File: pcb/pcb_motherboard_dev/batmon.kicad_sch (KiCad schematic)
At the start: 15 parts, among them U9 MCP6002-xSN

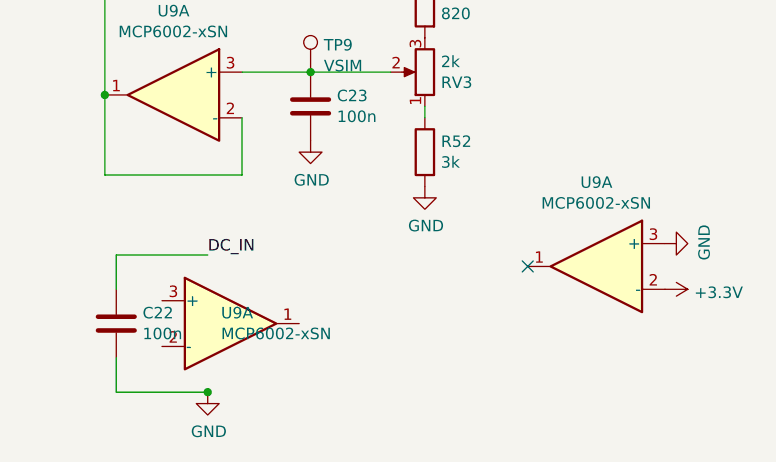
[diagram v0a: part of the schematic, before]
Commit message: PCB MB-DEV update
+Added a jumper for GPIO12 for flashing and setting efuse for 3.3 Flash operation
+Added Text Variables to Schematic and PCB
+introduced versioning of pcb
+added filenames and version to schematic sheets
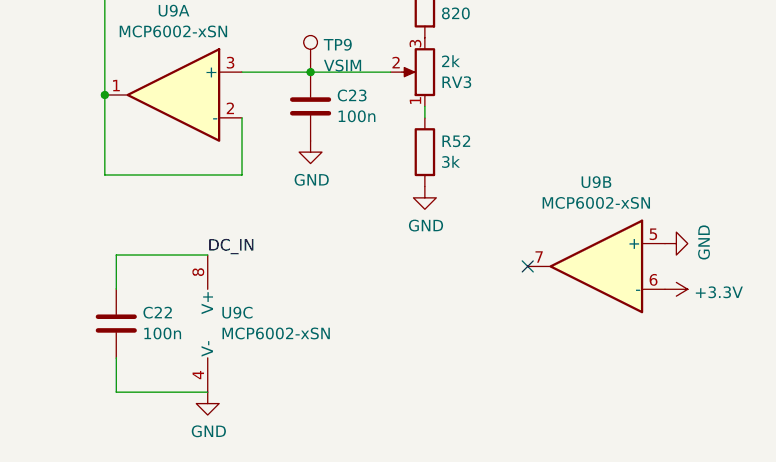
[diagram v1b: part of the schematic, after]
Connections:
- net +3V3: now also U9.6 (-); no longer U9.2 (-)
- net DC_IN: now also U9.8 (V+)
- net GND: now also U9.4 (V-), U9.5 (+); no longer U9.3 (+)
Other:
- title: (none) -> ForcelogADC_MB-DEV_v${VERSION}
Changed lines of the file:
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@@
 (kicad_sch (version 20211123) (generator eeschema)
   (paper "A4")
+  (title_block
+    (title "ForcelogADC_MB-DEV_v${VERSION}")
+    (rev "${REVISION}")
+  )
   (junction (at 105.41 88.9) (diameter 0) (color 0 0 0 0)
   )
@@
   )
   (junction (at 142.24 92.71) (diameter 0) (color 0 0 0 0)
-  )
-  (junction (at 153.67 125.73) (diameter 0) (color 0 0 0 0)
   )
   (no_connect (at 189.23 111.76))
@@
     (pin "1")
   )
-  (symbol (lib_id "Amplifier_Operational:MCP6002-xSN") (at 196.85 111.76 0) (mirror y)
+  (symbol (lib_id "Amplifier_Operational:MCP6002-xSN") (at 196.85 111.76 0) (mirror y) (unit 2)
     (in_bom yes) (on_board yes)
     (property "Reference" "U9" (id 0) (at 196.85 102.4382 0))
@@
       (effects (font (size 1.27 1.27)) hide)
     )
+    (pin "1")
+    (pin "2")
+    (pin "3")
     (pin "5")
     (pin "6")
     (pin "7")
-  )
-  (symbol (lib_id "power:GND") (at 204.47 109.22 90)
+    (pin "4")
+    (pin "8")
+  )
+  (symbol (lib_id "power:GND") (at 204.47 109.22 90) (unit 1)
     (in_bom yes) (on_board yes)
     (property "Reference" "#PWR0148" (id 0) (at 210.82 109.22 0)
@@
     (pin "1")
   )
-  (symbol (lib_id "Device:D_Schottky_Dual_Series_AKC") (at 105.41 83.82 0) (mirror y)
+  (symbol (lib_id "Device:D_Schottky_Dual_Series_AKC") (at 105.41 83.82 0) (mirror y) (unit 1)
     (in_bom yes) (on_board yes)
     (property "Reference" "D12" (id 0) (at 105.41 81.788 90)
@@
     (pin "3")
   )
-  (symbol (lib_id "power:GND") (at 113.03 83.82 90)
+  (symbol (lib_id "power:GND") (at 113.03 83.82 90) (unit 1)
     (in_bom yes) (on_board yes)
     (property "Reference" "#PWR0144" (id 0) (at 119.38 83.82 0)
@@
     (pin "1")
   )
-  (symbol (lib_id "Connector:TestPoint") (at 95.25 88.9 180)
+  (symbol (lib_id "Connector:TestPoint") (at 95.25 88.9 180) (unit 1)
     (in_bom yes) (on_board yes)
     (property "Reference" "TP8" (id 0) (at 96.7232 89.5604 0)
@@
     (pin "1")
   )
-  (symbol (lib_id "Connector:TestPoint") (at 165.1 90.17 0)
+  (symbol (lib_id "Connector:TestPoint") (at 165.1 90.17 0) (unit 1)
     (in_bom yes) (on_board yes)
     (property "Reference" "TP9" (id 0) (at 166.5732 87.1728 0)
@@
     (pin "1")
   )
-  (symbol (lib_id "Device:R") (at 121.92 82.55 0)
+  (symbol (lib_id "Device:R") (at 121.92 82.55 0) (unit 1)
     (in_bom yes) (on_board yes)
     (property "Reference" "R38" (id 0) (at 123.698 81.3816 0)
@@
     (pin "2")
   )
-  (symbol (lib_id "Device:R") (at 121.92 92.71 0)
+  (symbol (lib_id "Device:R") (at 121.92 92.71 0) (unit 1)
     (in_bom yes) (on_board yes)
     (property "Reference" "R39" (id 0) (at 123.698 91.5416 0)
@@
     (pin "2")
   )
-  (symbol (lib_id "Device:C") (at 110.49 92.71 0)
+  (symbol (lib_id "Device:C") (at 110.49 92.71 0) (unit 1)
     (in_bom yes) (on_board yes)
     (property "Reference" "C17" (id 0) (at 113.411 91.5416 0)
@@
     (pin "2")
   )
-  (symbol (lib_id "power:GND") (at 118.11 96.52 0)
+  (symbol (lib_id "power:GND") (at 118.11 96.52 0) (unit 1)
     (in_bom yes) (on_board yes)
     (property "Reference" "#PWR074" (id 0) (at 118.11 102.87 0)
@@
     (pin "1")
   )
-  (symbol (lib_id "Amplifier_Operational:MCP6002-xSN") (at 149.86 92.71 0) (mirror y)
+  (symbol (lib_id "Amplifier_Operational:MCP6002-xSN") (at 149.86 92.71 0) (mirror y) (unit 1)
     (in_bom yes) (on_board yes)
     (property "Reference" "U9" (id 0) (at 149.86 83.3882 0))
@@
     (pin "2")
     (pin "3")
-  )
-  (symbol (lib_id "Amplifier_Operational:MCP6002-xSN") (at 156.21 118.11 0)
-    (in_bom yes) (on_board yes)
-    (property "Reference" "U9" (id 0) (at 155.1432 116.9416 0)
-      (effects (font (size 1.27 1.27)) (justify left))
-    )
-    (property "Value" "MCP6002-xSN" (id 1) (at 155.1432 119.253 0)
-      (effects (font (size 1.27 1.27)) (justify left))
-    )
-    (property "Footprint" "Package_SO:SO-8_3.9x4.9mm_P1.27mm" (id 2) (at 156.21 118.11 0)
-      (effects (font (size 1.27 1.27)) hide)
-    )
-    (property "Datasheet" "http://ww1.microchip.com/downloads/en/DeviceDoc/21733j.pdf" (id 3) (at 156.21 118.11 0)
-      (effects (font (size 1.27 1.27)) hide)
-    )
-    (property "LCSC" "C7377" (id 4) (at 156.21 118.11 0)
-      (effects (font (size 1.27 1.27)) hide)
-    )
-    (property "Digikey" "MCP6002-I/SN-ND" (id 5) (at 156.21 118.11 0)
-      (effects (font (size 1.27 1.27)) hide)
-    )
+    (pin "5")
+    (pin "6")
+    (pin "7")
     (pin "4")
     (pin "8")
   )
-  (symbol (lib_id "Jumper:Jumper_3_Open") (at 121.92 74.93 0)
+  (symbol (lib_id "Amplifier_Operational:MCP6002-xSN") (at 156.21 118.11 0) (unit 3)
+    (in_bom yes) (on_board yes)
+    (property "Reference" "U9" (id 0) (at 155.1432 116.9416 0)
+      (effects (font (size 1.27 1.27)) (justify left))
+    )
+    (property "Value" "MCP6002-xSN" (id 1) (at 155.1432 119.253 0)
+      (effects (font (size 1.27 1.27)) (justify left))
+    )
+    (property "Footprint" "Package_SO:SO-8_3.9x4.9mm_P1.27mm" (id 2) (at 156.21 118.11 0)
+      (effects (font (size 1.27 1.27)) hide)
+    )
+    (property "Datasheet" "http://ww1.microchip.com/downloads/en/DeviceDoc/21733j.pdf" (id 3) (at 156.21 118.11 0)
+      (effects (font (size 1.27 1.27)) hide)
+    )
+    (property "LCSC" "C7377" (id 4) (at 156.21 118.11 0)
+      (effects (font (size 1.27 1.27)) hide)
+    )
+    (property "Digikey" "MCP6002-I/SN-ND" (id 5) (at 156.21 118.11 0)
+      (effects (font (size 1.27 1.27)) hide)
+    )
+    (pin "1")
+    (pin "2")
+    (pin "3")
+    (pin "5")
+    (pin "6")
+    (pin "7")
+    (pin "4")
+    (pin "8")
+  )
+  (symbol (lib_id "Jumper:Jumper_3_Open") (at 121.92 74.93 0) (unit 1)
     (in_bom yes) (on_board yes)
     (property "Reference" "JP3" (id 0) (at 121.92 71.5518 0))
@@
     (pin "3")
   )
-  (symbol (lib_id "Device:R_Potentiometer") (at 177.8 90.17 180)
+  (symbol (lib_id "Device:R_Potentiometer") (at 177.8 90.17 180) (unit 1)
     (in_bom yes) (on_board yes)
     (property "Reference" "RV3" (id 0) (at 179.578 91.3384 0)
@@
     (pin "3")
   )
-  (symbol (lib_id "Device:R") (at 177.8 82.55 0) (mirror y)
+  (symbol (lib_id "Device:R") (at 177.8 82.55 0) (mirror y) (unit 1)
     (in_bom yes) (on_board yes)
     (property "Reference" "R51" (id 0) (at 179.578 81.3816 0)
@@
     (pin "2")
   )
-  (symbol (lib_id "Device:R") (at 177.8 99.06 0) (mirror y)
+  (symbol (lib_id "Device:R") (at 177.8 99.06 0) (mirror y) (unit 1)
     (in_bom yes) (on_board yes)
     (property "Reference" "R52" (id 0) (at 179.578 97.8916 0)
@@
     (pin "2")
   )
-  (symbol (lib_id "power:GND") (at 177.8 102.87 0)
+  (symbol (lib_id "power:GND") (at 177.8 102.87 0) (unit 1)
     (in_bom yes) (on_board yes)
     (property "Reference" "#PWR083" (id 0) (at 177.8 109.22 0)
@@
     (pin "1")
   )
-  (symbol (lib_id "power:GND") (at 153.67 125.73 0)
+  (symbol (lib_id "power:GND") (at 153.67 125.73 0) (unit 1)
     (in_bom yes) (on_board yes)
     (property "Reference" "#PWR078" (id 0) (at 153.67 132.08 0)
@@
     (pin "1")
   )
-  (symbol (lib_id "Device:C") (at 165.1 93.98 0)
+  (symbol (lib_id "Device:C") (at 165.1 93.98 0) (unit 1)
     (in_bom yes) (on_board yes)
     (property "Reference" "C23" (id 0) (at 168.021 92.8116 0)
@@
     (pin "2")
   )
-  (symbol (lib_id "power:GND") (at 165.1 97.79 0)
+  (symbol (lib_id "power:GND") (at 165.1 97.79 0) (unit 1)
     (in_bom yes) (on_board yes)
     (property "Reference" "#PWR081" (id 0) (at 165.1 104.14 0)
@@
     (pin "1")
   )
-  (symbol (lib_id "Device:C") (at 143.51 118.11 0)
+  (symbol (lib_id "Device:C") (at 143.51 118.11 0) (unit 1)
     (in_bom yes) (on_board yes)
     (property "Reference" "C22" (id 0) (at 146.431 116.9416 0)
@@
     (pin "2")
   )
-  (symbol (lib_id "power:GND") (at 204.47 59.69 0)
+  (symbol (lib_id "power:GND") (at 204.47 59.69 0) (unit 1)
     (in_bom yes) (on_board yes)
     (property "Reference" "#PWR085" (id 0) (at 204.47 66.04 0)
